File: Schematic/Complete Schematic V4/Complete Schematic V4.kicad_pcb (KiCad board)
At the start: 2 copper layers, 73 parts, among them J1 Conn_Coaxial, J2 USB_A, J3 AudioJack3, U1 Si5351A-B-GT, U2 SN74CBT3253, U3 LT6231, U4 LT6231, U5 LM4562MA, U6 LM4562MA, Y1 Crystal_GND24_Small

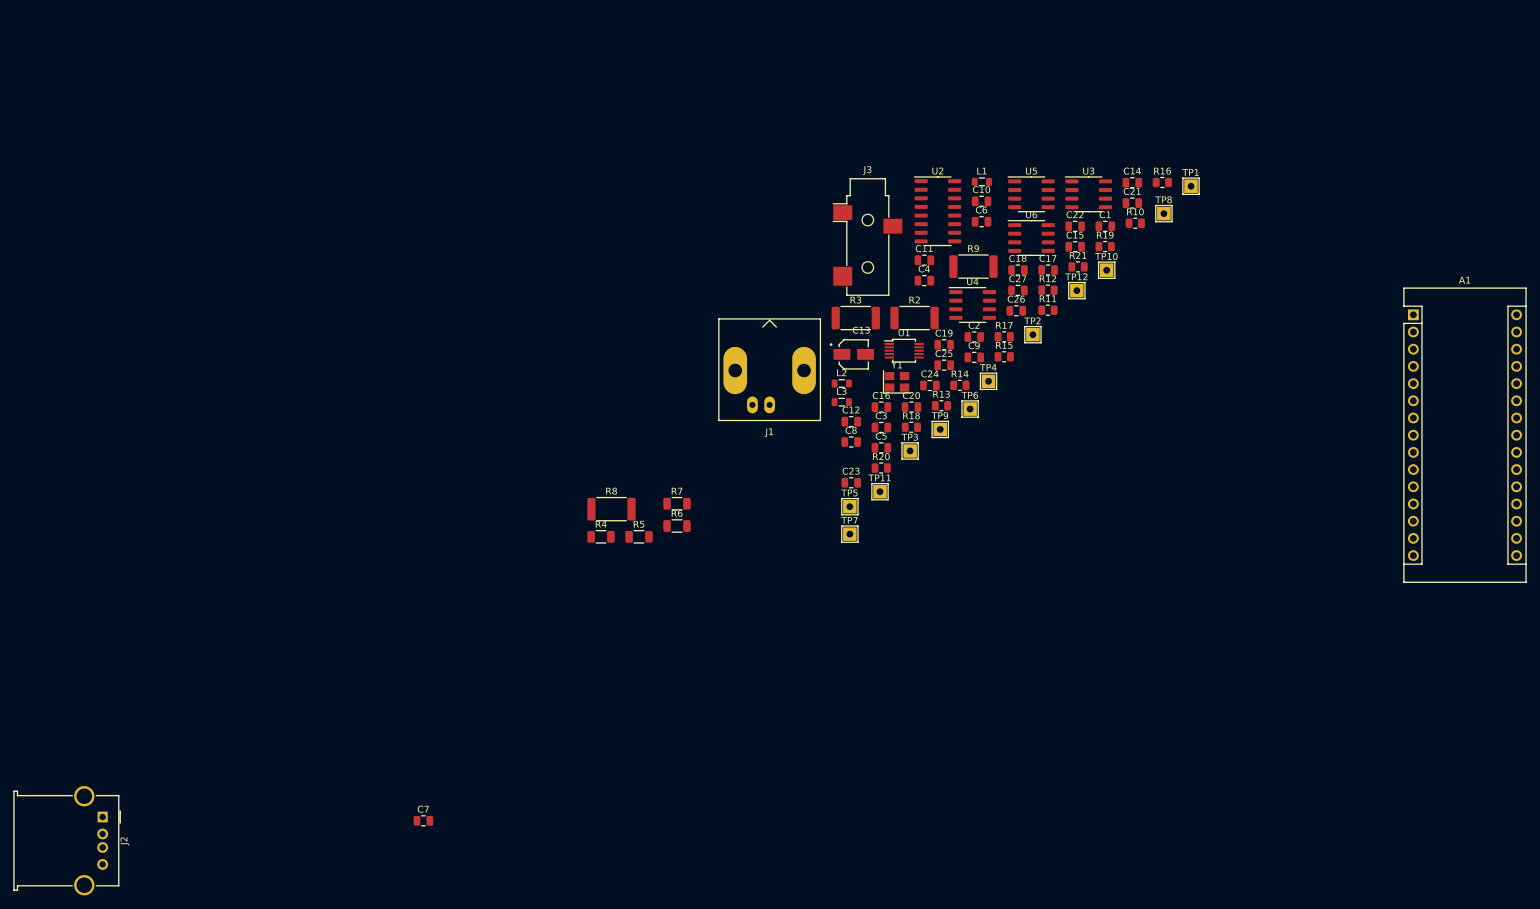
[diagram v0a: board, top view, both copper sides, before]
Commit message: Christian's PCB Work, But Josh's PCB Design is what we're using
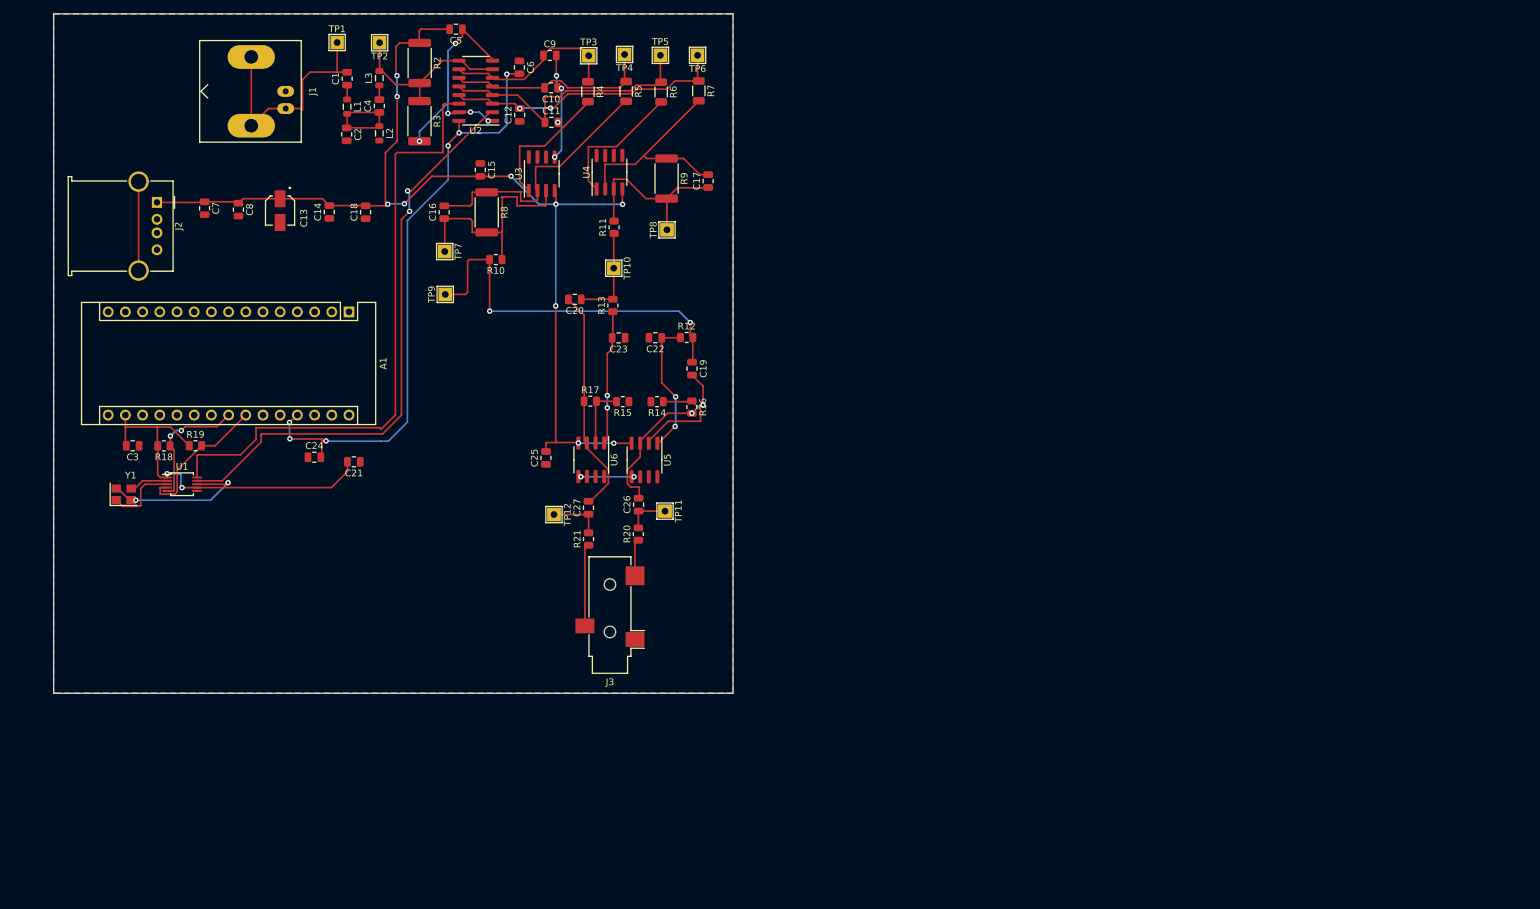
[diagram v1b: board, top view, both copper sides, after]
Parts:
- moved A1 157.2 mm to (74.1, 103.7), turned to -90 degrees
- moved R19 137.5 mm to (51.4, 123.5)
- moved TP1 127.9 mm to (72.3, 63.9)
- moved C21 121.2 mm to (74.8, 125.8), turned to 180 degrees
- moved C14 118.7 mm to (71.2, 89.0), turned to 90 degrees
- moved Y1 115.4 mm to (40.8, 130.6)
- moved C1 114.1 mm to (73.8, 69.3), turned to 90 degrees
- moved C3 110.6 mm to (42.2, 123.5), turned to 180 degrees
- moved R18 110.4 mm to (46.8, 123.5), turned to 180 degrees
- moved U1 108.4 mm to (49.5, 129.2)
- moved TP2 105.7 mm to (78.6, 64.0), turned to 180 degrees
- moved C2 97.4 mm to (73.8, 77.5), turned to -90 degrees
- moved C8 96.8 mm to (57.8, 88.6), turned to -90 degrees
- moved C18 96.7 mm to (76.5, 89.0), turned to 90 degrees
- moved C7 96.1 mm to (52.8, 88.4), turned to -90 degrees
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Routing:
- net Filtered 5V: track 0.00 -> 161.1 mm, vias 0 -> 10
- net Net-(U1-Pad10): track 0.00 -> 91.3 mm
- net GND: track 0.00 -> 90.8 mm, vias 0 -> 13
- net +5V: track 0.00 -> 90.1 mm, vias 0 -> 6
- net Net-(U1-Pad9): track 0.00 -> 86.0 mm, vias 0 -> 2
- net Net-(C19-Pad1): track 0.00 -> 55.4 mm, vias 0 -> 2
- net +3V3: track 0.00 -> 55.3 mm, vias 0 -> 2
- net Net-(C12-Pad2): track 0.00 -> 41.8 mm, vias 0 -> 2
- net Net-(C11-Pad1): track 0.00 -> 40.7 mm
- net Net-(C16-Pad2): track 0.00 -> 39.7 mm
- net Net-(C16-Pad1): track 0.00 -> 34.8 mm
- net Net-(C1-Pad2): track 0.00 -> 34.7 mm
- net Net-(C20-Pad2): track 0.00 -> 33.7 mm
- net Net-(C17-Pad2): track 0.00 -> 32.1 mm
- net Net-(C10-Pad2): track 0.00 -> 30.6 mm
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- added copper zone on B.Cu, net GND
- added copper zone on F.Cu, net GND
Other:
- board outline added: 100.3 x 100.3 mm
